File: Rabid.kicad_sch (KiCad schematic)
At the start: 223 parts, among them J1 USB Connector, J3 GPIO Debug Header, SW1 Esc, SW10 A, SW100 Unused, SW101 Unused, SW102 →, SW103 BootSel Switch, SW104 Reset Switch, SW11 Z, SW12 LMeta, SW13 F1, SW14 2, SW15 W, SW16 S, SW17 X, SW18 LAlt, SW19 F2, SW2 Tilde, SW20 3, SW21 E, SW22 D, SW23 C, SW24 Unused, SW25 F3, SW26 4, SW27 R, SW28 F, SW29 V, SW3 Tab, SW30 Unused, SW31 F4, SW32 5, SW33 T, SW34 G, SW35 B, SW36 Unused, SW37 F5, SW38 6, SW39 Y, SW4 CapsLk, SW40 H, SW41 N, SW42 Space, SW43 F6, SW44 7, SW45 U, SW46 J, SW47 M, SW48 Unused, SW49 F7, SW5 LShift, SW50 8, SW51 I, SW52 K, SW53 ,, SW54 Unused, SW55 F8, SW56 9, SW57 O, SW58 L, SW59 ., SW6 LCtrl, SW60 Unused, SW61 F9, SW62 0, SW63 P, SW64 ;, SW65 /, SW66 AltGr, SW67 F10, SW68 -, SW69 [, SW7 Unused, SW70 ", SW71 RShift, SW72 RMeta, SW73 F11, SW74 =, SW75 ]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

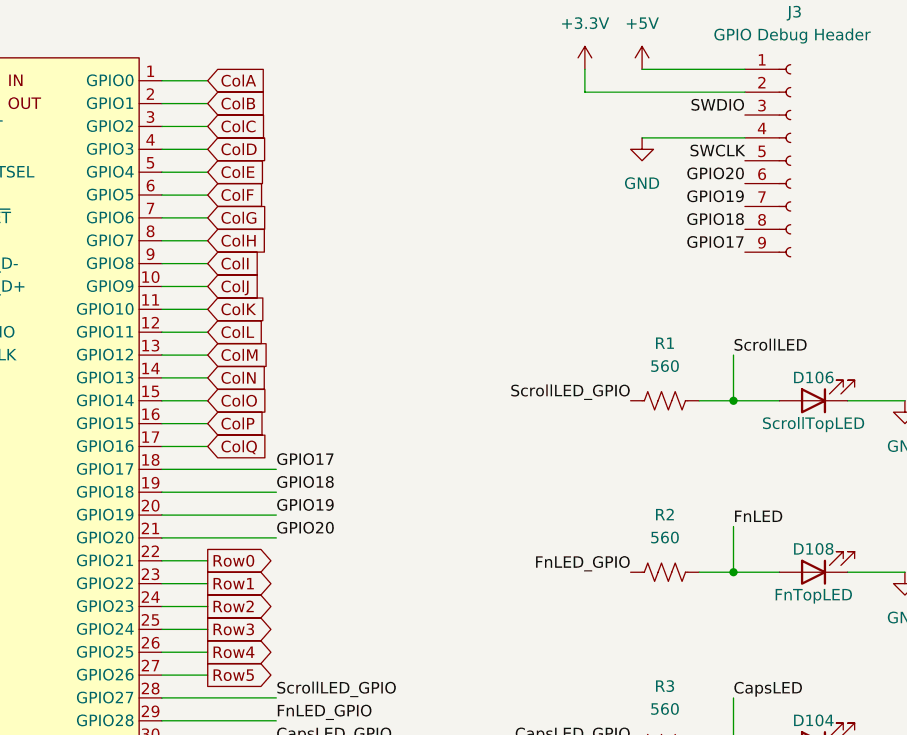
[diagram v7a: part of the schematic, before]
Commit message: Swap GPIO20 and GPIO21 (ROW0) pins.
The RP2040 Stamp has a WS2812B LED on the GPIO21 line.
It does have a jumper to disable the LED, but better to just work
around it, so it remains usable.
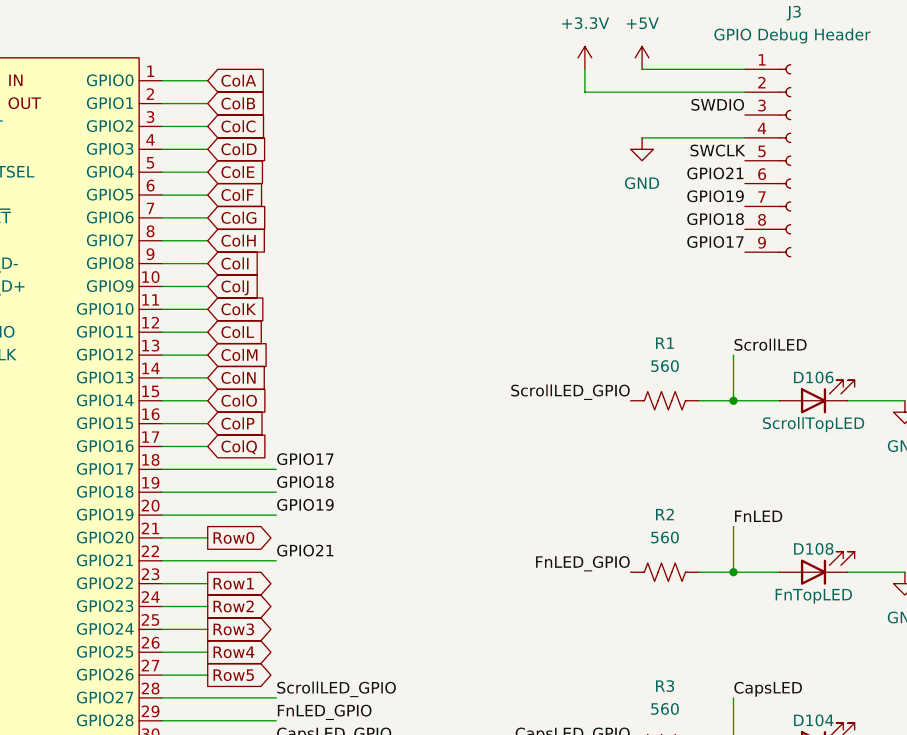
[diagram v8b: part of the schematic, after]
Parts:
- U1: footprint RP2040_Stamp:RP2040_Stamp_SMD -> RP2040_Stamp:RP2040_Stamp_THT
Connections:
- net Row0: now also U1.21 (GPIO20); no longer U1.22 (GPIO21)
- net GPIO20 renamed GPIO21
- net GPIO21: now also U1.22 (GPIO21); no longer U1.21 (GPIO20)
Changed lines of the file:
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@@
     (stroke (width 0) (type default) (color 0 0 0 0))
   )
-  (wire (pts (xy 100.33 236.22) (xy 95.25 236.22))
-    (stroke (width 0) (type default) (color 0 0 0 0))
-  )
   (wire (pts (xy 205.74 73.66) (xy 205.74 80.01))
     (stroke (width 0) (type default) (color 0 0 0 0))
@@
     (stroke (width 0) (type default) (color 0 0 0 0))
   )
-  (wire (pts (xy 107.95 233.68) (xy 95.25 233.68))
-    (stroke (width 0) (type default) (color 0 0 0 0))
-  )
   (wire (pts (xy 223.52 54.61) (xy 223.52 67.31))
     (stroke (width 0) (type default) (color 0 0 0 0))
@@
     (stroke (width 0) (type default) (color 0 0 0 0))
   )
+  (wire (pts (xy 107.95 236.22) (xy 95.25 236.22))
+    (stroke (width 0) (type default) (color 0 0 0 0))
+  )
   (wire (pts (xy 63.5 73.66) (xy 83.82 73.66))
     (stroke (width 0) (type default) (color 0 0 0 0))
@@
     (stroke (width 0) (type default) (color 0 0 0 0))
   )
+  (wire (pts (xy 100.33 233.68) (xy 95.25 233.68))
+    (stroke (width 0) (type default) (color 0 0 0 0))
+  )
   (wire (pts (xy 142.24 54.61) (xy 142.24 67.31))
     (stroke (width 0) (type default) (color 0 0 0 0))
@@
     (effects (font (size 1.27 1.27)) (justify right bottom))
   )
-  (label "GPIO20" (at 107.95 233.68 0)
+  (label "GPIO21" (at 107.95 236.22 0)
     (effects (font (size 1.27 1.27)) (justify left bottom))
   )
@@
     (effects (font (size 1.27 1.27)) (justify left bottom))
   )
-  (label "GPIO20" (at 160.02 194.31 180)
+  (label "GPIO21" (at 160.02 194.31 180)
     (effects (font (size 1.27 1.27)) (justify right bottom))
   )
@@
     )
   )
-  (global_label "Row0" (shape output) (at 100.33 236.22 0) (fields_autoplaced)
+  (global_label "Row0" (shape output) (at 100.33 233.68 0) (fields_autoplaced)
     (effects (font (size 1.27 1.27)) (justify left))
-    (property "Intersheet References" "${INTERSHEET_REFS}" (id 0) (at 107.7021 236.2994 0)
+    (property "Intersheet References" "${INTERSHEET_REFS}" (id 0) (at 107.7021 233.7594 0)
       (effects (font (size 1.27 1.27)) (justify right) hide)
     )
@@
       (effects (font (size 1.27 1.27)) (justify left))
     )
-    (property "Footprint" "RP2040_Stamp:RP2040_Stamp_SMD" (id 2) (at 82.55 262.89 0)
+    (property "Footprint" "RP2040_Stamp:RP2040_Stamp_THT" (id 2) (at 82.55 262.89 0)
       (effects (font (size 1.27 1.27)) hide)
     )
@@
     )
     (path "/192f83a9-3726-4136-83ac-7fa10874c246"
-      (reference "U1") (unit 1) (value "RP2040_Stamp") (footprint "RP2040_Stamp:RP2040_Stamp_SMD")
+      (reference "U1") (unit 1) (value "RP2040_Stamp") (footprint "RP2040_Stamp:RP2040_Stamp_THT")
     )
   )
